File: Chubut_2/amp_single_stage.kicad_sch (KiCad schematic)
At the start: 5 parts, among them U8 PSA4-5043+

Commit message: First version of final version
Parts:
- added C20: 10u, Capacitor_SMD:C_0805_2012Metric, symbol Device:C
- added R17: 10 ohm, Resistor_SMD:R_0402_1005Metric, symbol Device:R
- renumbered C33 to C21, C35 to C22, C34 to C23, L8 to L4, U8 to U4
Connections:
- net 3-5V: now also C20.1, R17.1; no longer C22.1, L4.1
- net GND: now also C20.2
- new net: C22.1, L4.1, R17.2
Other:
- moved on the sheet: C22
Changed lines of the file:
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@@
 (kicad_sch (version 20211123) (generator eeschema)
   (paper "A4")
-  (junction (at 149.86 86.36) (diameter 0) (color 0 0 0 0)
+  (junction (at 135.89 80.01) (diameter 0) (color 0 0 0 0)
   )
   (junction (at 149.86 106.68) (diameter 0) (color 0 0 0 0)
   )
-  (wire (pts (xy 149.86 86.36) (xy 149.86 90.17))
+  (junction (at 123.19 80.01) (diameter 0) (color 0 0 0 0)
+  )
+  (wire (pts (xy 149.86 80.01) (xy 149.86 90.17))
     (stroke (width 0) (type default) (color 0 0 0 0))
   )
@@
     (stroke (width 0) (type default) (color 0 0 0 0))
   )
-  (wire (pts (xy 149.86 86.36) (xy 165.1 86.36))
-    (stroke (width 0) (type default) (color 0 0 0 0))
-  )
   (wire (pts (xy 149.86 106.68) (xy 154.94 106.68))
     (stroke (width 0) (type default) (color 0 0 0 0))
   )
+  (wire (pts (xy 135.89 80.01) (xy 149.86 80.01))
+    (stroke (width 0) (type default) (color 0 0 0 0))
+  )
+  (wire (pts (xy 133.35 80.01) (xy 135.89 80.01))
+    (stroke (width 0) (type default) (color 0 0 0 0))
+  )
+  (wire (pts (xy 123.19 80.01) (xy 123.19 81.28))
+    (stroke (width 0) (type default) (color 0 0 0 0))
+  )
   (wire (pts (xy 149.86 97.79) (xy 149.86 106.68))
     (stroke (width 0) (type default) (color 0 0 0 0))
@@
     (stroke (width 0) (type default) (color 0 0 0 0))
   )
+  (wire (pts (xy 115.57 80.01) (xy 123.19 80.01))
+    (stroke (width 0) (type default) (color 0 0 0 0))
+  )
+  (wire (pts (xy 123.19 80.01) (xy 125.73 80.01))
+    (stroke (width 0) (type default) (color 0 0 0 0))
+  )
   (wire (pts (xy 168.91 106.68) (xy 162.56 106.68))
     (stroke (width 0) (type default) (color 0 0 0 0))
@@
     (stroke (width 0) (type default) (color 0 0 0 0))
   )
-  (wire (pts (xy 143.51 86.36) (xy 149.86 86.36))
+  (wire (pts (xy 135.89 80.01) (xy 135.89 81.28))
     (stroke (width 0) (type default) (color 0 0 0 0))
   )
@@
     (effects (font (size 1.27 1.27)) (justify left))
   )
-  (hierarchical_label "3-5V" (shape input) (at 143.51 86.36 180)
+  (hierarchical_label "3-5V" (shape input) (at 115.57 80.01 180)
     (effects (font (size 1.27 1.27)) (justify right))
   )
@@
     (effects (font (size 1.27 1.27)) (justify right))
   )
+  (symbol (lib_id "Device:C") (at 123.19 85.09 0)
+    (in_bom yes) (on_board yes) (fields_autoplaced)
+    (property "Reference" "C20" (id 0) (at 127.254 83.8199 0)
+      (effects (font (size 1.27 1.27)) (justify left))
+    )
+    (property "Value" "10u" (id 1) (at 127.254 86.3599 0)
+      (effects (font (size 1.27 1.27)) (justify left))
+    )
+    (property "Footprint" "Capacitor_SMD:C_0805_2012Metric" (id 2) (at 124.1552 88.9 0)
+      (effects (font (size 1.27 1.27)) hide)
+    )
+    (property "Datasheet" "~" (id 3) (at 123.19 85.09 0)
+      (effects (font (size 1.27 1.27)) hide)
+    )
+    (pin "1")
+    (pin "2")
+  )
   (symbol (lib_id "Device:C") (at 158.75 106.68 90)
     (in_bom yes) (on_board yes) (fields_autoplaced)
-    (property "Reference" "C34" (id 0) (at 158.75 98.806 90))
+    (property "Reference" "C23" (id 0) (at 158.75 98.806 90))
     (property "Value" "10n" (id 1) (at 158.75 101.346 90))
     (property "Footprint" "Capacitor_SMD:C_0402_1005Metric" (id 2) (at 162.56 105.7148 0)
@@
   (symbol (lib_id "power:GND") (at 140.97 114.3 0)
     (in_bom yes) (on_board yes) (fields_autoplaced)
-    (property "Reference" "#PWR049" (id 0) (at 140.97 120.65 0)
+    (property "Reference" "#PWR038" (id 0) (at 140.97 120.65 0)
       (effects (font (size 1.27 1.27)) hide)
     )
@@
     (pin "1")
   )
-  (symbol (lib_id "power:GND") (at 165.1 93.98 0)
-    (in_bom yes) (on_board yes) (fields_autoplaced)
-    (property "Reference" "#PWR050" (id 0) (at 165.1 100.33 0)
-      (effects (font (size 1.27 1.27)) hide)
-    )
-    (property "Value" "GND" (id 1) (at 165.1 98.806 0))
-    (property "Footprint" "" (id 2) (at 165.1 93.98 0)
-      (effects (font (size 1.27 1.27)) hide)
-    )
-    (property "Datasheet" "" (id 3) (at 165.1 93.98 0)
+  (symbol (lib_id "power:GND") (at 135.89 88.9 0)
+    (in_bom yes) (on_board yes) (fields_autoplaced)
+    (property "Reference" "#PWR037" (id 0) (at 135.89 95.25 0)
+      (effects (font (size 1.27 1.27)) hide)
+    )
+    (property "Value" "GND" (id 1) (at 135.89 93.726 0))
+    (property "Footprint" "" (id 2) (at 135.89 88.9 0)
+      (effects (font (size 1.27 1.27)) hide)
+    )
+    (property "Datasheet" "" (id 3) (at 135.89 88.9 0)
       (effects (font (size 1.27 1.27)) hide)
     )
@@
   (symbol (lib_id "Device:L") (at 149.86 93.98 0)
     (in_bom yes) (on_board yes) (fields_autoplaced)
-    (property "Reference" "L8" (id 0) (at 151.13 92.7099 0)
+    (property "Reference" "L4" (id 0) (at 151.13 92.7099 0)
       (effects (font (size 1.27 1.27)) (justify left))
     )
@@
     (pin "2")
   )
+  (symbol (lib_id "Device:R") (at 129.54 80.01 90)
+    (in_bom yes) (on_board yes) (fields_autoplaced)
+    (property "Reference" "R17" (id 0) (at 129.54 73.66 90))
+    (property "Value" "10 ohm" (id 1) (at 129.54 76.2 90))
+    (property "Footprint" "Resistor_SMD:R_0402_1005Metric" (id 2) (at 129.54 81.788 90)
+      (effects (font (size 1.27 1.27)) hide)
+    )
+    (property "Datasheet" "~" (id 3) (at 129.54 80.01 0)
+      (effects (font (size 1.27 1.27)) hide)
+    )
+    (pin "1")
+    (pin "2")
+  )
   (symbol (lib_id "Chubut2:PSA4-5043+") (at 140.97 102.87 0)
     (in_bom yes) (on_board yes) (fields_autoplaced)
-    (property "Reference" "U8" (id 0) (at 140.97 98.806 0))
+    (property "Reference" "U4" (id 0) (at 140.97 98.806 0))
     (property "Value" "PSA4-5043+" (id 1) (at 140.97 101.346 0))
     (property "Footprint" "chubut:MMM1362" (id 2) (at 140.97 102.87 0)
@@
     (pin "4")
   )
-  (symbol (lib_id "Device:C") (at 165.1 90.17 0)
-    (in_bom yes) (on_board yes) (fields_autoplaced)
-    (property "Reference" "C35" (id 0) (at 169.164 88.8999 0)
-      (effects (font (size 1.27 1.27)) (justify left))
-    )
-    (property "Value" "10u" (id 1) (at 169.164 91.4399 0)
-      (effects (font (size 1.27 1.27)) (justify left))
-    )
-    (property "Footprint" "Capacitor_SMD:C_0805_2012Metric" (id 2) (at 166.0652 93.98 0)
-      (effects (font (size 1.27 1.27)) hide)
-    )
-    (property "Datasheet" "~" (id 3) (at 165.1 90.17 0)
-      (effects (font (size 1.27 1.27)) hide)
-    )
-    (pin "1")
-    (pin "2")
+  (symbol (lib_id "Device:C") (at 135.89 85.09 0)
+    (in_bom yes) (on_board yes) (fields_autoplaced)
+    (property "Reference" "C22" (id 0) (at 139.954 83.8199 0)
+      (effects (font (size 1.27 1.27)) (justify left))
+    )
+    (property "Value" "10u" (id 1) (at 139.954 86.3599 0)
+      (effects (font (size 1.27 1.27)) (justify left))
+    )
+    (property "Footprint" "Capacitor_SMD:C_0805_2012Metric" (id 2) (at 136.8552 88.9 0)
+      (effects (font (size 1.27 1.27)) hide)
+    )
+    (property "Datasheet" "~" (id 3) (at 135.89 85.09 0)
+      (effects (font (size 1.27 1.27)) hide)
+    )
+    (pin "1")
+    (pin "2")
+  )
+  (symbol (lib_id "power:GND") (at 123.19 88.9 0)
+    (in_bom yes) (on_board yes) (fields_autoplaced)
+    (property "Reference" "#PWR036" (id 0) (at 123.19 95.25 0)
+      (effects (font (size 1.27 1.27)) hide)
+    )
+    (property "Value" "GND" (id 1) (at 123.19 93.726 0))
+    (property "Footprint" "" (id 2) (at 123.19 88.9 0)
+      (effects (font (size 1.27 1.27)) hide)
+    )
+    (property "Datasheet" "" (id 3) (at 123.19 88.9 0)
+      (effects (font (size 1.27 1.27)) hide)
+    )
+    (pin "1")
   )
   (symbol (lib_id "Device:C") (at 124.46 106.68 90)
     (in_bom yes) (on_board yes) (fields_autoplaced)
-    (property "Reference" "C33" (id 0) (at 124.46 98.806 90))
+    (property "Reference" "C21" (id 0) (at 124.46 98.806 90))
     (property "Value" "10n" (id 1) (at 124.46 101.346 90))
     (property "Footprint" "Capacitor_SMD:C_0402_1005Metric" (id 2) (at 128.27 105.7148 0)

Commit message: Not sure what is this
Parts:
- renumbered C20 to C36, C21 to C37, C22 to C38, C23 to C39, L4 to L8, R17 to R25, U4 to U8
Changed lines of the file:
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@@
   (symbol (lib_id "Device:C") (at 123.19 85.09 0)
     (in_bom yes) (on_board yes) (fields_autoplaced)
-    (property "Reference" "C20" (id 0) (at 127.254 83.8199 0)
+    (property "Reference" "C36" (id 0) (at 127.254 83.8199 0)
       (effects (font (size 1.27 1.27)) (justify left))
     )
@@
   (symbol (lib_id "Device:C") (at 158.75 106.68 90)
     (in_bom yes) (on_board yes) (fields_autoplaced)
-    (property "Reference" "C23" (id 0) (at 158.75 98.806 90))
+    (property "Reference" "C39" (id 0) (at 158.75 98.806 90))
     (property "Value" "10n" (id 1) (at 158.75 101.346 90))
     (property "Footprint" "Capacitor_SMD:C_0402_1005Metric" (id 2) (at 162.56 105.7148 0)
@@
   (symbol (lib_id "power:GND") (at 140.97 114.3 0)
     (in_bom yes) (on_board yes) (fields_autoplaced)
-    (property "Reference" "#PWR038" (id 0) (at 140.97 120.65 0)
+    (property "Reference" "#PWR054" (id 0) (at 140.97 120.65 0)
       (effects (font (size 1.27 1.27)) hide)
     )
@@
   (symbol (lib_id "power:GND") (at 135.89 88.9 0)
     (in_bom yes) (on_board yes) (fields_autoplaced)
-    (property "Reference" "#PWR037" (id 0) (at 135.89 95.25 0)
+    (property "Reference" "#PWR053" (id 0) (at 135.89 95.25 0)
       (effects (font (size 1.27 1.27)) hide)
     )
@@
   (symbol (lib_id "Device:L") (at 149.86 93.98 0)
     (in_bom yes) (on_board yes) (fields_autoplaced)
-    (property "Reference" "L4" (id 0) (at 151.13 92.7099 0)
+    (property "Reference" "L8" (id 0) (at 151.13 92.7099 0)
       (effects (font (size 1.27 1.27)) (justify left))
     )
@@
   (symbol (lib_id "Device:R") (at 129.54 80.01 90)
     (in_bom yes) (on_board yes) (fields_autoplaced)
-    (property "Reference" "R17" (id 0) (at 129.54 73.66 90))
+    (property "Reference" "R25" (id 0) (at 129.54 73.66 90))
     (property "Value" "10 ohm" (id 1) (at 129.54 76.2 90))
     (property "Footprint" "Resistor_SMD:R_0402_1005Metric" (id 2) (at 129.54 81.788 90)
@@
   (symbol (lib_id "Chubut2:PSA4-5043+") (at 140.97 102.87 0)
     (in_bom yes) (on_board yes) (fields_autoplaced)
-    (property "Reference" "U4" (id 0) (at 140.97 98.806 0))
+    (property "Reference" "U8" (id 0) (at 140.97 98.806 0))
     (property "Value" "PSA4-5043+" (id 1) (at 140.97 101.346 0))
     (property "Footprint" "chubut:MMM1362" (id 2) (at 140.97 102.87 0)
@@
   (symbol (lib_id "Device:C") (at 135.89 85.09 0)
     (in_bom yes) (on_board yes) (fields_autoplaced)
-    (property "Reference" "C22" (id 0) (at 139.954 83.8199 0)
+    (property "Reference" "C38" (id 0) (at 139.954 83.8199 0)
       (effects (font (size 1.27 1.27)) (justify left))
     )
@@
   (symbol (lib_id "power:GND") (at 123.19 88.9 0)
     (in_bom yes) (on_board yes) (fields_autoplaced)
-    (property "Reference" "#PWR036" (id 0) (at 123.19 95.25 0)
+    (property "Reference" "#PWR052" (id 0) (at 123.19 95.25 0)
       (effects (font (size 1.27 1.27)) hide)
     )
@@
   (symbol (lib_id "Device:C") (at 124.46 106.68 90)
     (in_bom yes) (on_board yes) (fields_autoplaced)
-    (property "Reference" "C21" (id 0) (at 124.46 98.806 90))
+    (property "Reference" "C37" (id 0) (at 124.46 98.806 90))
     (property "Value" "10n" (id 1) (at 124.46 101.346 90))
     (property "Footprint" "Capacitor_SMD:C_0402_1005Metric" (id 2) (at 128.27 105.7148 0)

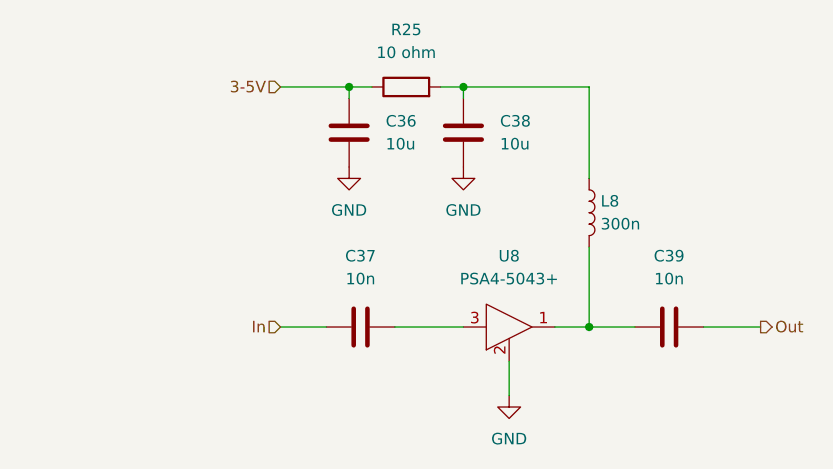
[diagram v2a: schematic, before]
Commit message: Implemented modifications suggested by the workshop
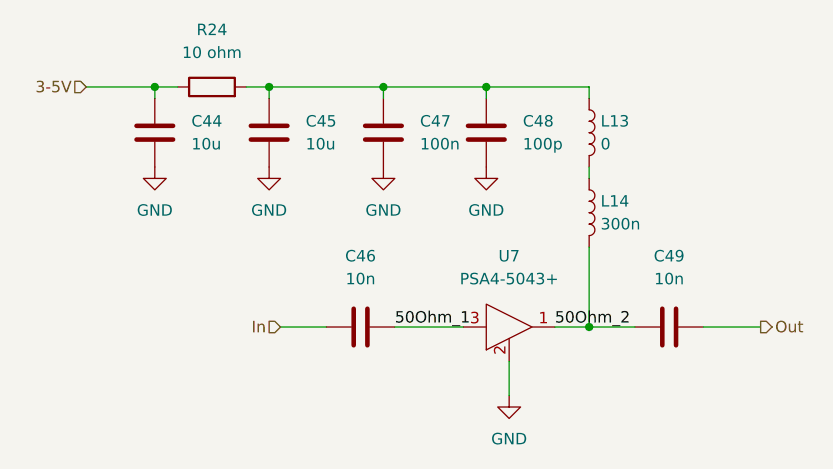
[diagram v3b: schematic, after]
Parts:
- added C47: 100n, Capacitor_SMD:C_0402_1005Metric, symbol Device:C
- added C48: 100p, Capacitor_SMD:C_0402_1005Metric, symbol Device:C
- added L13: 0, Inductor_SMD:L_0402_1005Metric, symbol Device:L
- C44: renamed from C36; footprint Capacitor_SMD:C_0805_2012Metric -> Capacitor_SMD:C_0402_1005Metric
- C45: renamed from C38; footprint Capacitor_SMD:C_0805_2012Metric -> Capacitor_SMD:C_0402_1005Metric
- renumbered C37 to C46, C39 to C49, L8 to L14, R25 to R24, U8 to U7
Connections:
- net GND: now also C47.2, C48.2
- net 50Ohm_2: now reaches C49.1, L14.2, U7.1 (RF-OUT_and_DC-IN)
- net at C45.1, R24.2: now also C47.1, C48.1, L13.1; no longer L14.1
- net 50Ohm_1: now reaches C46.2, U7.3 (RF-IN)
- new net: L13.2, L14.1
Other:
- moved on the sheet: C44, C45, R24

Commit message: Fixed capacitor value
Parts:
- C28: renamed from C46; value 10n -> 1n
- C31: renamed from C49; value 10n -> 1n
- renumbered C44 to C26, C45 to C27, C47 to C29, C48 to C30, L13 to L7, L14 to L8, R24 to R17, U7 to U4
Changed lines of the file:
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@@
   (symbol (lib_id "Device:C") (at 127 85.09 0)
     (in_bom yes) (on_board yes) (fields_autoplaced)
-    (property "Reference" "C47" (id 0) (at 131.064 83.8199 0)
+    (property "Reference" "C29" (id 0) (at 131.064 83.8199 0)
       (effects (font (size 1.27 1.27)) (justify left))
     )
@@
   (symbol (lib_id "Device:C") (at 101.6 85.09 0)
     (in_bom yes) (on_board yes) (fields_autoplaced)
-    (property "Reference" "C44" (id 0) (at 105.664 83.8199 0)
+    (property "Reference" "C26" (id 0) (at 105.664 83.8199 0)
       (effects (font (size 1.27 1.27)) (justify left))
     )
@@
   (symbol (lib_id "Device:C") (at 158.75 106.68 90)
     (in_bom yes) (on_board yes) (fields_autoplaced)
-    (property "Reference" "C49" (id 0) (at 158.75 98.806 90))
-    (property "Value" "10n" (id 1) (at 158.75 101.346 90))
+    (property "Reference" "C31" (id 0) (at 158.75 99.06 90))
+    (property "Value" "1n" (id 1) (at 158.75 101.6 90))
     (property "Footprint" "Capacitor_SMD:C_0402_1005Metric" (id 2) (at 162.56 105.7148 0)
       (effects (font (size 1.27 1.27)) hide)
@@
   (symbol (lib_id "power:GND") (at 127 88.9 0)
     (in_bom yes) (on_board yes) (fields_autoplaced)
-    (property "Reference" "#PWR063" (id 0) (at 127 95.25 0)
+    (property "Reference" "#PWR045" (id 0) (at 127 95.25 0)
       (effects (font (size 1.27 1.27)) hide)
     )
@@
   (symbol (lib_id "power:GND") (at 140.97 114.3 0)
     (in_bom yes) (on_board yes) (fields_autoplaced)
-    (property "Reference" "#PWR065" (id 0) (at 140.97 120.65 0)
+    (property "Reference" "#PWR047" (id 0) (at 140.97 120.65 0)
       (effects (font (size 1.27 1.27)) hide)
     )
@@
   (symbol (lib_id "power:GND") (at 138.43 88.9 0)
     (in_bom yes) (on_board yes) (fields_autoplaced)
-    (property "Reference" "#PWR064" (id 0) (at 138.43 95.25 0)
+    (property "Reference" "#PWR046" (id 0) (at 138.43 95.25 0)
       (effects (font (size 1.27 1.27)) hide)
     )
@@
   (symbol (lib_id "Device:L") (at 149.86 85.09 0)
     (in_bom yes) (on_board yes) (fields_autoplaced)
-    (property "Reference" "L13" (id 0) (at 151.13 83.8199 0)
+    (property "Reference" "L7" (id 0) (at 151.13 83.8199 0)
       (effects (font (size 1.27 1.27)) (justify left))
     )
@@
   (symbol (lib_id "power:GND") (at 114.3 88.9 0)
     (in_bom yes) (on_board yes) (fields_autoplaced)
-    (property "Reference" "#PWR062" (id 0) (at 114.3 95.25 0)
+    (property "Reference" "#PWR044" (id 0) (at 114.3 95.25 0)
       (effects (font (size 1.27 1.27)) hide)
     )
@@
   (symbol (lib_id "Device:L") (at 149.86 93.98 0)
     (in_bom yes) (on_board yes) (fields_autoplaced)
-    (property "Reference" "L14" (id 0) (at 151.13 92.7099 0)
+    (property "Reference" "L8" (id 0) (at 151.13 92.7099 0)
       (effects (font (size 1.27 1.27)) (justify left))
     )
@@
   (symbol (lib_id "Device:R") (at 107.95 80.01 90)
     (in_bom yes) (on_board yes) (fields_autoplaced)
-    (property "Reference" "R24" (id 0) (at 107.95 73.66 90))
+    (property "Reference" "R17" (id 0) (at 107.95 73.66 90))
     (property "Value" "10 ohm" (id 1) (at 107.95 76.2 90))
     (property "Footprint" "Resistor_SMD:R_0402_1005Metric" (id 2) (at 107.95 81.788 90)
@@
   (symbol (lib_id "Chubut2:PSA4-5043+") (at 140.97 102.87 0)
     (in_bom yes) (on_board yes) (fields_autoplaced)
-    (property "Reference" "U7" (id 0) (at 140.97 98.806 0))
+    (property "Reference" "U4" (id 0) (at 140.97 98.806 0))
     (property "Value" "PSA4-5043+" (id 1) (at 140.97 101.346 0))
     (property "Footprint" "chubut:MMM1362" (id 2) (at 140.97 102.87 0)
@@
   (symbol (lib_id "Device:C") (at 138.43 85.09 0)
     (in_bom yes) (on_board yes) (fields_autoplaced)
-    (property "Reference" "C48" (id 0) (at 142.494 83.8199 0)
+    (property "Reference" "C30" (id 0) (at 142.494 83.8199 0)
       (effects (font (size 1.27 1.27)) (justify left))
     )
@@
   (symbol (lib_id "Device:C") (at 114.3 85.09 0)
     (in_bom yes) (on_board yes) (fields_autoplaced)
-    (property "Reference" "C45" (id 0) (at 118.364 83.8199 0)
+    (property "Reference" "C27" (id 0) (at 118.364 83.8199 0)
       (effects (font (size 1.27 1.27)) (justify left))
     )
@@
   (symbol (lib_id "power:GND") (at 101.6 88.9 0)
     (in_bom yes) (on_board yes) (fields_autoplaced)
-    (property "Reference" "#PWR061" (id 0) (at 101.6 95.25 0)
+    (property "Reference" "#PWR043" (id 0) (at 101.6 95.25 0)
       (effects (font (size 1.27 1.27)) hide)
     )
@@
   (symbol (lib_id "Device:C") (at 124.46 106.68 90)
     (in_bom yes) (on_board yes) (fields_autoplaced)
-    (property "Reference" "C46" (id 0) (at 124.46 98.806 90))
-    (property "Value" "10n" (id 1) (at 124.46 101.346 90))
+    (property "Reference" "C28" (id 0) (at 124.46 98.806 90))
+    (property "Value" "1n" (id 1) (at 124.46 101.346 90))
     (property "Footprint" "Capacitor_SMD:C_0402_1005Metric" (id 2) (at 128.27 105.7148 0)
       (effects (font (size 1.27 1.27)) hide)

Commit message: Converted files to KiCAD 7
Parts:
- renumbered C26 to C44, C27 to C45, C28 to C46, C29 to C47, C30 to C48, C31 to C49, L7 to L13, L8 to L14, R17 to R24, U4 to U7
